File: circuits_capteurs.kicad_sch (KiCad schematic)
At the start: 51 parts, among them U10 LMC6482IN, U13 INA2331AIPWR, U2 INA2331AIPWR, U3 LMC6482IN, U7 LMC6482IN, U9 LMC6482IN

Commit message: Schematic fini, en théorie
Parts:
- removed R1: 8k, symbol Device:R
- removed R11: 10k, symbol Device:R
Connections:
- removed net 1,8V: U7.6 (NEGB), U7.7 (OUTB), Vibe1.1 (VDD)
- net ADC1 renamed ADC1_INP16-Therm2
- net ADC2 renamed ADC12_INP3-Therm1
- net ADC3 renamed ADC12_INP14-SG1.2
- net ADC4 renamed ADC12_INP18-SG5.6
- net ADC5 renamed ADC12_INP15-SG3.4
- net ADC6 renamed ADC123_INP10-Vibro2
- net ADC7 renamed ADC3_INP1-Vibe1
- net POSB: no longer names the net of U7.5 (POSB)
- new net: SG1. (Out), SG2. (Out)
- new net: SG5. (Out), SG6. (Out)
- new net: SG3. (Out), SG4. (Out)
- new net +1V8: Vibe1.1 (VDD)
- no-connect marks 4 -> 7

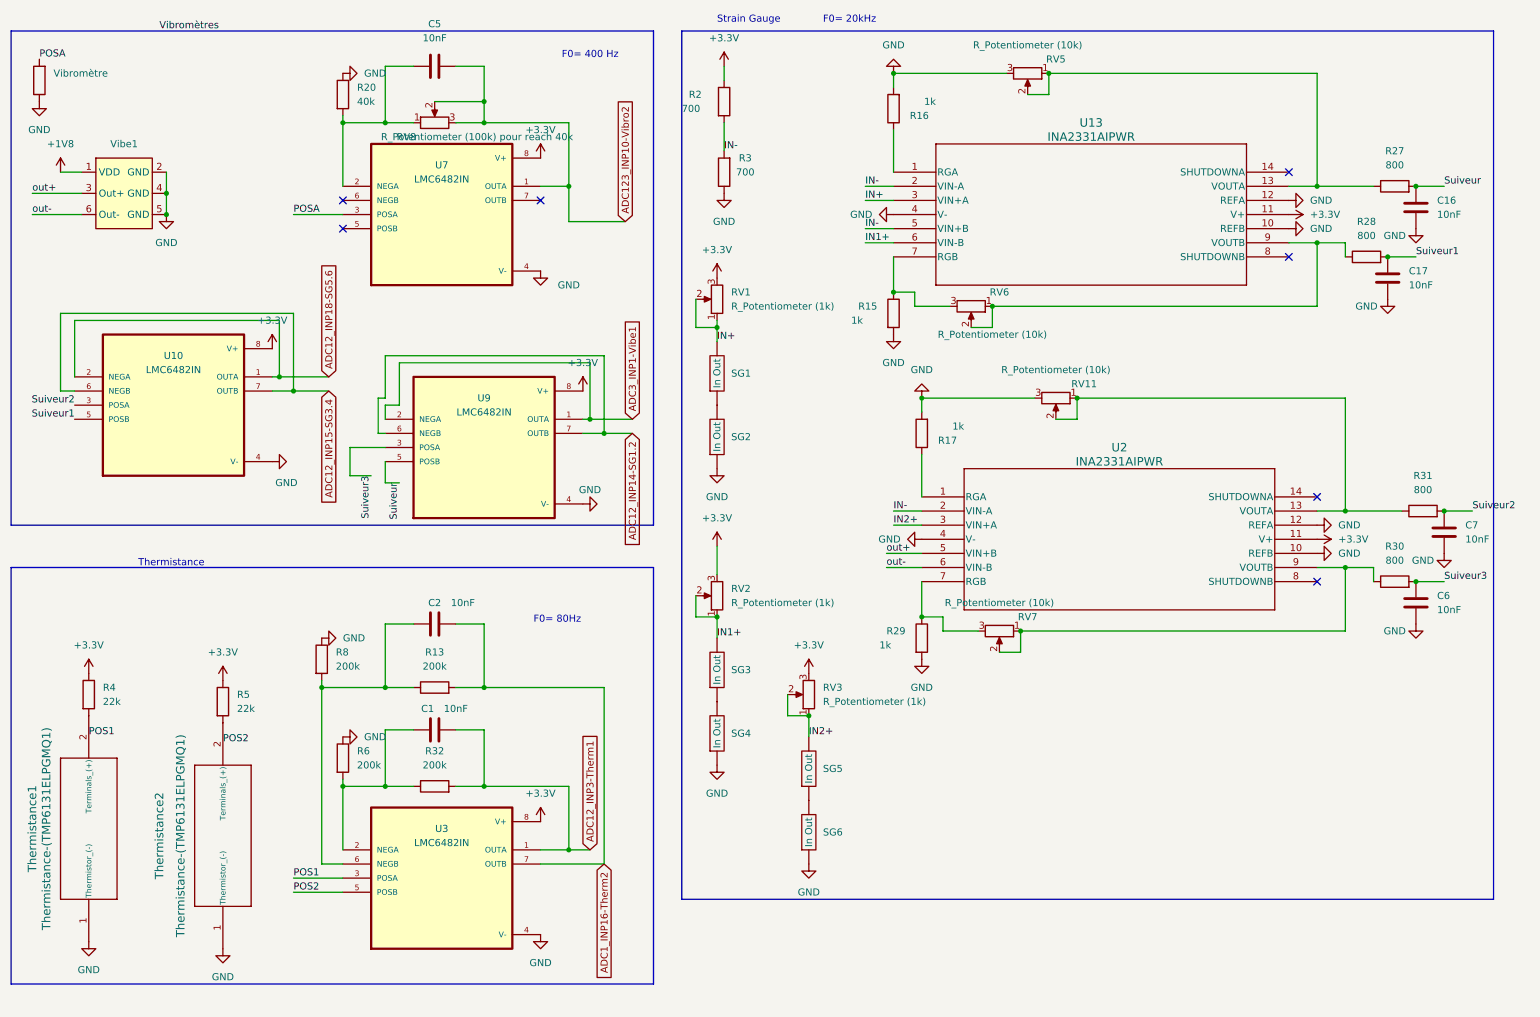
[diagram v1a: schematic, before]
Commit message: Petites modif et assignation des empreintes à 50%
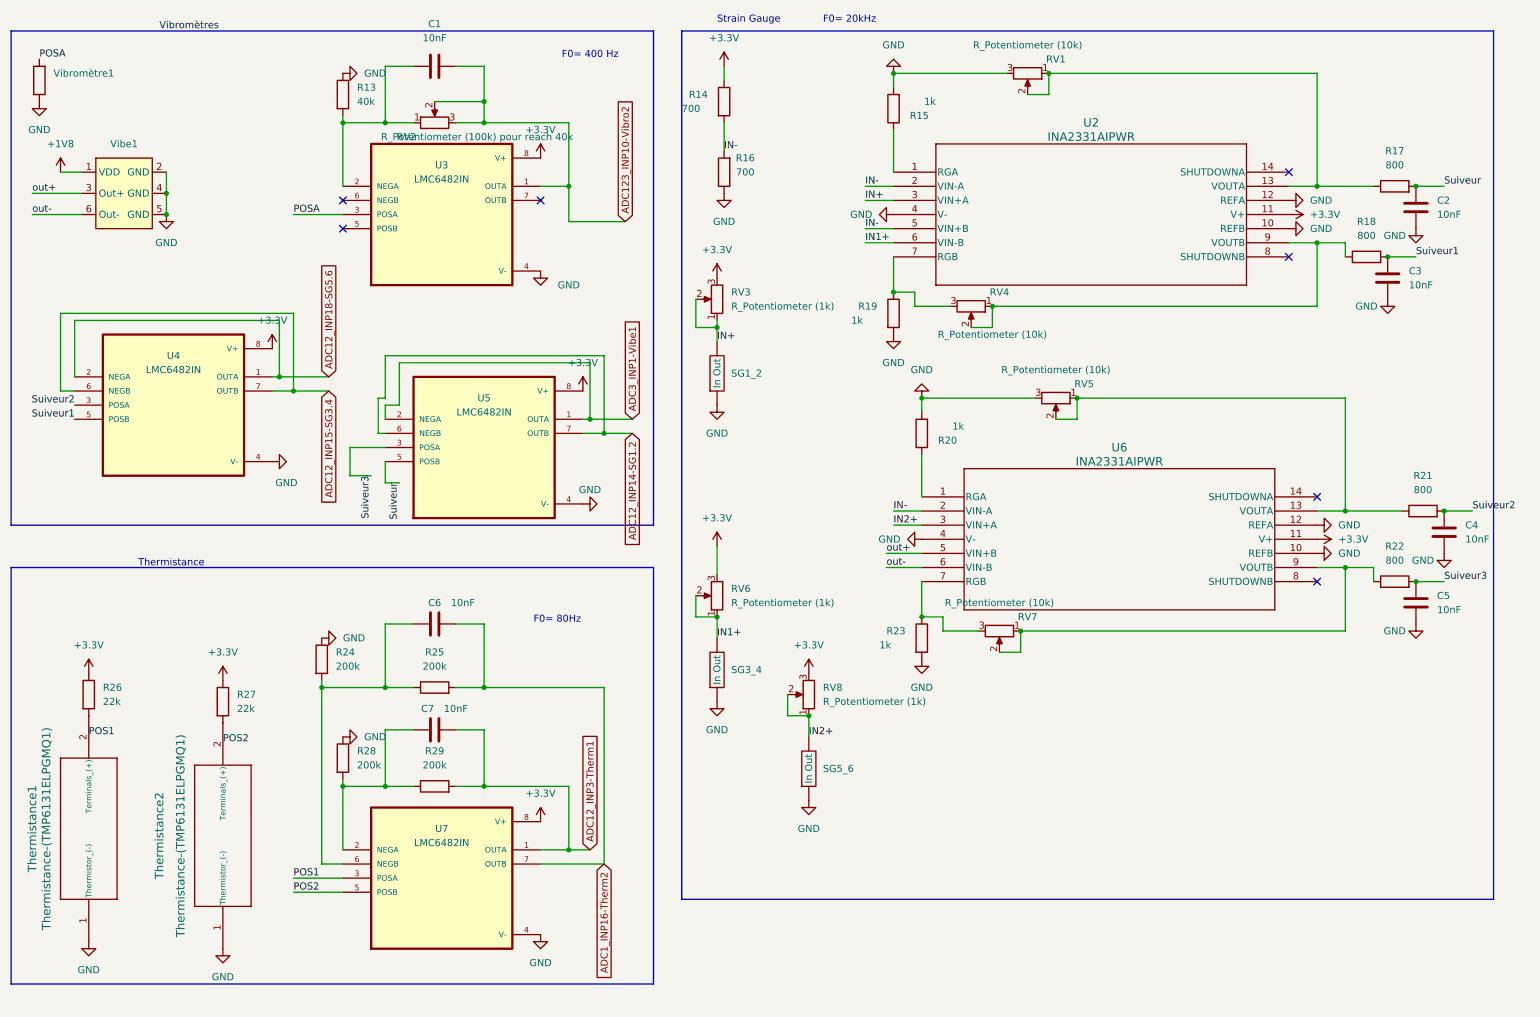
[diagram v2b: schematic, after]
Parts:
- removed SG1, SG2, SG4, SG6: ~, symbol GAUL-Symboles:Strain_Gauge
- R13: renamed from R20; footprint (none) -> Resistor_SMD:R_0603_1608Metric
- R14: renamed from R2; footprint (none) -> Resistor_SMD:R_0603_1608Metric
- R15: renamed from R16; footprint (none) -> Resistor_SMD:R_0603_1608Metric
- R16: renamed from R3; footprint (none) -> Resistor_SMD:R_0603_1608Metric
- R17: renamed from R27; footprint (none) -> Resistor_SMD:R_0603_1608Metric
- R18: renamed from R28; footprint (none) -> Resistor_SMD:R_0603_1608Metric
- R19: renamed from R15; footprint (none) -> Resistor_SMD:R_0603_1608Metric
- R20: renamed from R17; footprint (none) -> Resistor_SMD:R_0603_1608Metric
- R21: renamed from R31; footprint (none) -> Resistor_SMD:R_0603_1608Metric
- R22: renamed from R30; footprint (none) -> Resistor_SMD:R_0603_1608Metric
- R23: renamed from R29; footprint (none) -> Resistor_SMD:R_0603_1608Metric
- R24: renamed from R8; footprint (none) -> Resistor_SMD:R_0603_1608Metric
- R25: renamed from R13; footprint (none) -> Resistor_SMD:R_0603_1608Metric
- R26: renamed from R4; footprint (none) -> Resistor_SMD:R_0603_1608Metric
- R27: renamed from R5; footprint (none) -> Resistor_SMD:R_0603_1608Metric
- R28: renamed from R6; footprint (none) -> Resistor_SMD:R_0603_1608Metric
- R29: renamed from R32; footprint (none) -> Resistor_SMD:R_0603_1608Metric
- RV1: renamed from RV5; footprint (none) -> GAUL-Empreintes:trim_pot_debout-(RES3_66W)
- RV2: renamed from RV8; footprint (none) -> GAUL-Empreintes:trim_pot_debout-(RES3_66W)
- RV3: renamed from RV1; footprint (none) -> GAUL-Empreintes:trim_pot_debout-(RES3_66W)
- RV4: renamed from RV6; footprint (none) -> GAUL-Empreintes:trim_pot_debout-(RES3_66W)
- RV5: renamed from RV11; footprint (none) -> GAUL-Empreintes:trim_pot_debout-(RES3_66W)
- RV6: renamed from RV2; footprint (none) -> GAUL-Empreintes:trim_pot_debout-(RES3_66W)
- RV7: footprint (none) -> GAUL-Empreintes:trim_pot_debout-(RES3_66W)
- RV8: renamed from RV3; footprint (none) -> GAUL-Empreintes:trim_pot_debout-(RES3_66W)
- U2: renamed from U13; footprint PW14 -> GAUL-Empreintes:INA2331
- U6: renamed from U2; footprint PW14 -> GAUL-Empreintes:INA2331
- Vibe1: footprint (none) -> GAUL-Empreintes:Vibromètre
- renumbered C5 to C1, C16 to C2, C17 to C3, C7 to C4, C6 to C5, C2 to C6, C1 to C7, SG1 to SG1_2, SG3 to SG3_4, SG5 to SG5_6, U7 to U3, U10 to U4, U9 to U5, U3 to U7, Vibromètre to Vibromètre1
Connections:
- net GND: now also SG1_2. (Out), SG3_4. (Out), SG5_6. (Out)

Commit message: Début PCB
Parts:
- removed SG1_2, SG3_4, SG5_6: ~, symbol GAUL-Symboles:Strain_Gauge
- removed Thermistance1, Thermistance2: Thermistance-(TMP6131ELPGMQ1), symbol GAUL-Symboles:Thermistance-(TMP6131ELPGMQ1)
- removed Vibromètre1: 1k, symbol Device:R
- C1, C2, C3, C4, C5, C6, C7: footprint (none) -> Capacitor_SMD:C_0603_1608Metric_Pad1.08x0.95mm_HandSolder
- U3, U4, U5, U7: footprint LMC6482IN:DIP794W45P254L959H508Q8 -> GAUL-Empreintes:LMC6482-SMD-(SOP65P490X110-8N)
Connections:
- net POS1 is gone; now on net Therm1: U7.3 (POSA)
- net POS2 is gone; now on net Therm2: U7.5 (POSB)
- net Therm2: now reaches R27.2
- net Therm1: now reaches R26.2
- net IN+ renamed SG1_2
- net IN1+ renamed SG3_4
- net IN2+ renamed SG5_6
- net POSA renamed Vibro1
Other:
- note added: "vibromètres"
- moved on the sheet: R26

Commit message: PCB1
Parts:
- added C39, C40, C41, C42, C43, C44: 10nF, Capacitor_SMD:C_0603_1608Metric_Pad1.08x0.95mm_HandSolder, symbol Device:C
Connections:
- net +3.3V: now also C39.1, C40.1, C41.2, C42.1, C43.1, C44.1
- net GND: now also C39.2, C40.2, C41.1, C42.2, C43.2, C44.2; no longer RV1.3, RV5.3
- net at R20.1, U6.1 (RGA): now also RV5.3
- net at R15.1, U2.1 (RGA): now also RV1.3
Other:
- moved on the sheet: C3, C5, R18, R22
